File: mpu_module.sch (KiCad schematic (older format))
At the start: 1 part

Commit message: Added Mipi Dsi connection, started stlink module
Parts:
- added R7, R8: 4k7, Resistor_Smd_0603:4k7_0603, symbol Resistors_Smd0603:4k7
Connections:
- net GND: now reaches SOM1.1 (GND)
- net GND: now also SOM1.103 (GND), SOM1.107 (GND), SOM1.115 (GND), SOM1.116 (GND), SOM1.120 (GND), SOM1.125 (GND), SOM1.127 (GND), SOM1.128 (GND), SOM1.130 (GND), SOM1.132 (GND), SOM1.135 (GND), SOM1.136 (GND), SOM1.146 (GND), SOM1.147 (GND), SOM1.15 (GND), SOM1.156 (GND), SOM1.159 (GND), SOM1.165 (GND), SOM1.168 (GND), SOM1.17 (GND), SOM1.170 (GND), SOM1.172 (GND), SOM1.174 (GND), SOM1.176 (GND), SOM1.177 (GND), SOM1.178 (GND), SOM1.180 (GND), SOM1.181 (GND), SOM1.182 (GND), SOM1.184 (GND), SOM1.185 (GND), SOM1.189 (GND), SOM1.199 (GND), SOM1.2 (GND), SOM1.20 (GND), SOM1.200 (GND), SOM1.22 (GND), SOM1.23 (GND), SOM1.26 (GND), SOM1.28 (GND), SOM1.29 (GND), SOM1.35 (GND), SOM1.38 (GND), SOM1.40 (GND), SOM1.41 (GND), SOM1.50 (GND), SOM1.51 (GND), SOM1.59 (GND), SOM1.60 (GND), SOM1.70 (GND), SOM1.71 (GND), SOM1.81 (GND), SOM1.82 (GND), SOM1.84 (GND)
- net at SOM1.100 (+5VIN): now also SOM1.102 (+5VIN), SOM1.104 (+5VIN), SOM1.106 (+5VIN), SOM1.108 (+5VIN), SOM1.110 (+5VIN), SOM1.112 (+5VIN), SOM1.96 (+5VIN), SOM1.98 (+5VIN)
- net at SOM1.85 (+3.3VOUT): now also SOM1.87 (+3.3VOUT), SOM1.88 (+3.3VOUT), SOM1.89 (+3.3VOUT), SOM1.90 (+3.3VOUT), SOM1.91 (+3.3VOUT), SOM1.92 (+3.3VOUT), SOM1.93 (+3.3VOUT)
- net PA14_IRQ: now reaches SOM1.117 (PA14_DBTRGO,DBTRGI,MCO2,EVENTOUT)
- net PA1_GPIO: now reaches SOM1.157 (PA1_ETH_CLK,TIM2_CH2,TIM5_CH2,LPTIM3_OUT,TIM15_CH1N,USART2_RTS/USART2_DE,UART4_RX,QUADSPI_BK1_IO3,SAI2_MCLK_B,ETH1_GMII_RX_CLK/ETH1_MII_RX_CLK/ETH1_RGMII_RX_CLK/ETH1_RMII_REF_CLK,LCD_R2,EVENTOUT,ADC1_INP17,ADC1_INN16)
- net PE2_I2C4_SDA: now reaches SOM1.56 (PB7_TIM17_CH1N,TIM4_CH2,I2C1_SDA,I2C4_SDA,USART1_RX,SDMMC2_D1,DFSDM1_CKIN5,FMC_NL,DCMI_VSYNC,EVENTOUT)
- net PE2_I2C4_SDA: now also R7.2
- net PE2_I2C4_SCL: now reaches SOM1.121 (PE2_TRACECLK,SAI1_CK1,I2C4_SCL,SPI4_SCK,SAI1_MCLK_A,QUADSPI_BK1_IO2,ETH1_GMII_TXD3/ETH1_MII_TXD3/ETH1_RGMII_TXD3,FMC_A23,EVENTOUT)
- net PE2_I2C4_SCL: now also R8.2
- net MIPI_DSI_D0_N: now reaches SOM1.186 (DSI_D0N)
- net MIPI_DSI_D0_P: now reaches SOM1.188 (DSI_D0P)
- net MIPI_DSI_D1_N: now reaches SOM1.192 (DSI_D1N)
- net MIPI_DSI_CLK_N: now reaches SOM1.193 (DSI_CKN)
- net MIPI_DSI_D1_P: now reaches SOM1.194 (DSI_D1P)
- net MIPI_DSI_CLK_P: now reaches SOM1.195 (DSI_CKP)
- new net 3V3: R7.1, R8.1
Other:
- moved on the sheet: SOM1A, SOM1D, SOM1E, SOM1F, SOM1G, SOM1H

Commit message: Schematic finished, elements figurated on pcb, tracking started
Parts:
- added C55, C56: 100n, Capacitors_Smd_0603:100nF_0603, symbol Capacitors_Smd0603:100n
- added R51, R52, R53, R54, R55, R56: 10k, Resistor_Smd_0603:10k_0603, symbol Resistors_Smd0603:10k
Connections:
- net 3V3: now also R51.1, R53.1, R55.1
- net 5V: now also SOM1.100 (+5VIN), SOM1.102 (+5VIN), SOM1.104 (+5VIN), SOM1.106 (+5VIN), SOM1.108 (+5VIN), SOM1.110 (+5VIN), SOM1.112 (+5VIN), SOM1.96 (+5VIN), SOM1.98 (+5VIN)
- net GND: now also C55.2, C56.2, R52.2, R54.2, R56.2
- net PD13_MIPI_DSI_TE: now also SOM1.49 (PD13_LPTIM1_OUT,TIM4_CH2,I2C4_SDA,I2C1_SDA,I2S3_MCK,QUADSPI_BK1_IO3,SAI2_SCK_A,FMC_A18,DSI_TE,EVENTOUT)
- net PD15_TIM4_PWM_CH4: now also SOM1.111 (PD15_TIM4_CH4,SAI3_MCLK_A,UART8_CTS,FMC_D1/FMC_DA1,LCD_R1,EVENTOUT)
- net at SOM1.6 (VDD_3V3): now also C55.1
- net at SOM1.8 (VDD_COIN_3V): now also C56.1
- net at SOM1.10 (BOOT2): now also R55.2, R56.1
- net STM32-~RST~: now reaches SOM1.4 (STM32_nRST)
- net JTAG-TMS: now reaches SOM1.46 (JTAG_TMS)
- net JTAG-~TRST~: now reaches SOM1.48 (JTAG_nTRST)
- net JTAG-TDO: now reaches SOM1.52 (JTAG_TDO)
- net JTAG-TCK: now reaches SOM1.54 (JTAG_TCK)
- net at SOM1.7 (BOOT1): now also R53.2, R54.1
- net at SOM1.9 (BOOT0): now also R51.2, R52.1
- net USB-OTG1-D_P: now reaches SOM1.19 (USB_OTG1_DP)
- net USB-OTG1-D_M: now reaches SOM1.21 (USB_OTG1_DN)
- net USB-OTG2-D_P: now reaches SOM1.25 (USB_OTG2_DP)
- net USB-OTG2-D_M: now reaches SOM1.27 (USB_OTG2_DN)
- net ENET1-CRS-DV: now reaches SOM1.101 (PA7_TIM1_CH1N,TIM3_CH2,TIM8_CH1N,SAI4_D1,SPI1_MOSI/I2S1_SDO,SPI6_MOSI,TIM14_CH1,QUADSPI_CLK,ETH1_GMII_RX_DV/ETH1_MII_RX_DV/ETH1_RGMII_RX_CTL/ETH1_RMII_CRS_DV,SAI4_SD_A,_EVENTOUT,ADC1_INP7,ADC1_INN3,ADC2_INP7,ADC2_INN3)
- net PA13-GPIO: now reaches SOM1.113 (PA13_DBTRGO,DBTRGI,MCO1,UART4_TX,EVENTOUT,BOOTFAILN)
- net PA9-GPIO: now reaches SOM1.129 (PA9_TIM1_CH2,I2C3_SMBA,SPI2_SCK/I2S2_CK,USART1_TX,SDMMC2_CDIR,SDMMC2_D5,DCMI_D0,LCD_R5,EVENTOUT)
- net PA8-GPIO: now reaches SOM1.131 (PA8_MCO1,TIM1_CH1,TIM8_BKIN2,I2C3_SCL,SPI3_MOSI/I2S3_SDO,USART1_CK,SDMMC2_CKIN,SDMMC2_D4,OTG_FS_SOF/OTG_HS_SOF,SAI4_SD_B,UART7_RX,LCD_R6,EVENTOUT,)
- net ADC1_INP19: now reaches SOM1.140 (PA5_TIM2_CH1/TIM2_ETR,TIM8_CH1N,SAI4_CK1,SPI1_SCK/I2S1_CK,SPI6_SCK,SAI4_MCLK_A,LCD_R4,EVENTOUT,ADC1_INP19,ADC1_INN18,ADC2_INP19,ADC2_INN18,DAC_OUT2)
- net ADC1_INP15: now reaches SOM1.149 (PA3_TIM2_CH4,TIM5_CH4,LPTIM5_OUT,TIM15_CH2,USART2_RX,LCD_B2,ETH1_GMII_COL/ETH1_MII_COL,LCD_B5,EVENTOUT,ADC1_INP15,PVD_IN)
- net ADC1_INP3: now reaches SOM1.152 (PA6_TIM1_BKIN,TIM3_CH1,TIM8_BKIN,SAI4_CK2,SPI1_MISO/I2S1_SDI,SPI6_MISO,TIM13_CH1,MDIOS_MDC,SAI4_SCK_A,DCMI_PIXCLK,LCD_G2,EVENTOUT,ADC1_INP3,ADC2_INP3)
- net SPI1_NSS: now reaches SOM1.162 (PA4_HDP0,TIM5_ETR,SAI4_D2,SPI1_NSS/I2S1_WS,SPI3_NSS/I2S3_WS,USART2_CK,SPI6_NSS,SAI4_FS_A,DCMI_HSYNC,LCD_VSYNC,EVENTOUT,ADC1_INP18,ADC2_INP18,DAC_OUT1)
- net ENET1-MDIO: now reaches SOM1.61 (PA2_TIM2_CH3,TIM5_CH3,LPTIM4_OUT,TIM15_CH1,USART2_TX,SAI2_SCK_B,SDMMC2_D0DIR,_ETH1_MDIO,_MDIOS_MDIO,_LCD_R1,_EVENTOUT,_ADC1_INP14,_WKUP2)
- net PA0-GPIO: now reaches SOM1.62 (PA0_TIM2_CH1/TIM2_ETR,TIM5_CH1,TIM8_ETR,TIM15_BKIN,USART2_CTS/USART2_NSS,UART4_TX,SDMMC2_CMD,SAI2_SD_B,ETH1_GMII_CRS/ETH1_MII_CRS,EVENTOUT)
- net SPI3_NSS: now reaches SOM1.69 (PA10_TIM1_CH3,SPI3_NSS/I2S3_WS,USART1_RX,MDIOS_MDIO,SAI4_FS_B,DCMI_D1,LCD_B1,EVENTOUT,OTG_FS_ID,OTG_HS_ID)
- net I2C6-SCL: now reaches SOM1.76 (PA11_TIM1_CH4,I2C6_SCL,I2C5_SCL,SPI2_NSS/I2S2_WS,UART4_RX,USART1_CTS/USART1_NSS,FDCAN1_RX,LCD_R4,EVENTOUT,OTG_FS_DM)
- net I2C6-SDA: now reaches SOM1.80 (PA12_TIM1_ETR,I2C6_SDA,I2C5_SDA,UART4_TX,USART1_RTS/USART1_DE,SAI2_FS_B,FDCAN1_TX,LCD_R5,EVENTOUT,OTG_FS_DP)
- net ENET1-TX-EN: now reaches SOM1.114 (PB11_TIM2_CH4,LPTIM2_ETR,I2C2_SDA,DFSDM1_CKIN7,USART3_RX,ETH1_GMII_TX_EN/ETH1_MII_TX_EN/ETH1_RGMII_TX_CTL/ETH1_RMII_TX_EN,DSI_TE,LCD_G5,EVENTOUT)
- net SPI1_MOSI: now reaches SOM1.118 (PB5_ETH_CLK,TIM17_BKIN,TIM3_CH2,SAI4_D1,I2C1_SMBA,SPI1_MOSI/I2S1_SDO,I2C4_SMBA,SPI3_MOSI/I2S3_SDO,SPI6_MOSI,FDCAN2_RX,SAI4_SD_A,ETH1_PPS_OUT,UART5_RX,DCMI_D10,LCD_G7,EVENTOUT)
- net ENET1-TXD1: now reaches SOM1.124 (PB13_TIM1_CH1N,DFSDM1_CKOUT,LPTIM2_OUT,SPI2_SCK/I2S2_CK,DFSDM1_CKIN1,USART3_CTS/USART3_NSS,FDCAN2_TX,ETH1_GMII_TXD1/ETH1_MII_TXD1/ETH1_RGMII_TXD1/ETH1_RMII_TXD1,UART5_TX,EVENTOUT)
- net ENET1-RXD2: now reaches SOM1.138 (PB0_TIM1_CH2N,TIM3_CH3,TIM8_CH2N,DFSDM1_CKOUT,UART4_CTS,LCD_R3,ETH1_GMII_RXD2/ETH1_MII_RXD2/ETH1_RGMII_RXD2,MDIOS_MDIO,LCD_G1,EVENTOUT,ADC1_INP9,ADC1_INN5,ADC2_INP9,ADC2_INN5)
- net ENET1-RX-ER: now reaches SOM1.150 (PB10_TIM2_CH3,LPTIM2_IN1,I2C2_SCL,SPI2_SCK/I2S2_CK,DFSDM1_DATIN7,USART3_TX,QUADSPI_BK1_NCS,ETH1_GMII_RX_ER/ETH1_MII_RX_ER,LCD_G4,EVENTOUT)
- net ENET1-TXD3: now reaches SOM1.151 (PB8_HDP6,TIM16_CH1,TIM4_CH3,DFSDM1_CKIN7,I2C1_SCL,SDMMC1_CKIN,I2C4_SCL,SDMMC2_CKIN,UART4_RX,FDCAN1_RX,SDMMC2_D4,ETH1_GMII_TXD3/ETH1_MII_TXD3/ETH1_RGMII_TXD3,SDMMC1_D4,DCMI_D6,LCD_B6,_EVENTOUT)
- net I2C1-SDA: now reaches SOM1.166 (PB9_HDP7,TIM17_CH1,TIM4_CH4,DFSDM1_DATIN7,I2C1_SDA,SPI2_NSS/I2S2_WS,I2C4_SDA,SDMMC2_CDIR,UART4_TX,FDCAN1_TX,SDMMC2_D5,SDMMC1_CDIR,SDMMC1_D5,DCMI_D7,LCD_B7,EVENTOUT)
- net USART1-TXD: now reaches SOM1.167 (PB14_TIM1_CH2N,TIM12_CH1,TIM8_CH2N,USART1_TX,SPI2_MISO/I2S2_SDI,DFSDM1_DATIN2,USART3_RTS/USART3_DE,SDMMC2_D0,EVENTOUT)
- net SPI1_MISO: now reaches SOM1.169 (PB4_TRACED8,TIM16_BKIN,TIM3_CH1,SAI4_CK2,SPI1_MISO/I2S1_SDI,SPI3_MISO/I2S3_SDI,SPI2_NSS/I2S2_WS,SPI6_MISO,SDMMC2_D3,SAI4_SCK_A,UART7_TX,EVENTOUT)
- net USART1-RXD: now reaches SOM1.171 (PB15_RTC_REFIN,TIM1_CH3N,TIM12_CH2,TIM8_CH3N,USART1_RX,SPI2_MOSI/I2S2_SDO,DFSDM1_CKIN2,SDMMC2_D1,EVENTOUT)
- net SPI1_SCK: now reaches SOM1.175 (PB3_TRACED9,TIM2_CH2,SAI4_CK1,SPI1_SCK/I2S1_CK,SPI3_SCK/I2S3_CK,SPI6_SCK,SDMMC2_D2,SAI4_MCLK_A,UART7_RX,EVENTOUT)
- net ENET1-RXD3: now reaches SOM1.58 (PB1_TIM1_CH3N,TIM3_CH4,TIM8_CH3N,DFSDM1_DATIN1,LCD_R6,ETH1_GMII_RXD3/ETH1_MII_RXD3/ETH1_RGMII_RXD3,MDIOS_MDC,LCD_G0,EVENTOUT,ADC1_INP5,ADC2_INP5)
- net I2C1-SCL: now reaches SOM1.73 (PB6_TIM16_CH1N,TIM4_CH1,I2C1_SCL,_CEC,I2C4_SCL,USART1_TX,FDCAN2_TX,QUADSPI_BK1_NCS,DFSDM1_DATIN5,UART5_TX,DCMI_D5,EVENTOUT)
- net UART4-RXD: now reaches SOM1.77 (PB2_TRACED4,RTC_OUT2,SAI1_D1,DFSDM1_CKIN1,USART1_RX,I2S_CKIN,SAI1_SD_A,SPI3_MOSI/I2S3_SDO,UART4_RX,QUADSPI_CLK,EVENTOUT)
- net ENET1-TXD2: now reaches SOM1.119 (PC2_DFSDM1_CKIN1,SPI2_MISO/I2S2_SDI,DFSDM1_CKOUT,ETH1_GMII_TXD2/ETH1_MII_TXD2/ETH1_RGMII_TXD2,DCMI_PIXCLK,EVENTOUT,ADC1_INP12,ADC1_INN11)
- net SPI3_SCK: now reaches SOM1.137 (PC10_TRACED2,DFSDM1_CKIN5,SPI3_SCK/I2S3_CK,USART3_TX,UART4_TX,QUADSPI_BK1_IO1,SAI4_MCLK_B,SDMMC1_D2,DCMI_D8,LCD_R2,EVENTOUT)
- net PC7-GPIO: now reaches SOM1.141 (PC7_HDP4,TIM3_CH2,TIM8_CH2,DFSDM1_DATIN3,I2S3_MCK,USART6_RX,SDMMC1_D123DIR,SDMMC2_D123DIR,SDMMC2_D7,SDMMC1_D7,DCMI_D1,LCD_G6,EVENTOUT)
- net PC6-GPIO: now reaches SOM1.160 (PC6_HDP1,TIM3_CH1,TIM8_CH1,DFSDM1_CKIN3,I2S2_MCK,USART6_TX,SDMMC1_D0DIR,SDMMC2_D0DIR,SDMMC2_D6,DSI_TE,SDMMC1_D6,DCMI_D0,LCD_HSYNC,EVENTOUT)
- net ADC1_INP13: now reaches SOM1.47 (PC3_TRACECLK,DFSDM1_DATIN1,SPI2_MOSI/I2S2_SDO,ETH1_GMII_TX_CLK/ETH1_MII_TX_CLK,EVENTOUT,ADC1_INP13,ADC1_INN12)
- net ENET1-MDC: now reaches SOM1.53 (PC1_TRACED0,SAI1_D1,DFSDM1_DATIN0,DFSDM1_CKIN4,SPI2_MOSI/I2S2_SDO,SAI1_SD_A,SDMMC2_CK,ETH1_MDC,MDIOS_MDC,EVENTOUT,ADC1_INP11,ADC1_INN10,ADC2_INP11,ADC2_INN10,TAMP_IN3,WKUP6)
- net ADC2_INP10: now reaches SOM1.55 (PC0_DFSDM1_CKIN0,LPTIM2_IN2,DFSDM1_DATIN4,SAI2_FS_B,QUADSPI_BK2_NCS,LCD_R5,EVENTOUT,ADC1_INP10,ADC2_INP10)
- net ENET1-RXD0: now reaches SOM1.97 (PC4_DFSDM1_CKIN2,I2S1_MCK,SPDIFRX_IN2,ETH1_GMII_RXD0/ETH1_MII_RXD0/ETH1_RGMII_RXD0/ETH1_RMII_RXD0,EVENTOUT,ADC1_INP4,ADC2_INP4)
- net ENET1-RXD1: now reaches SOM1.99 (PC5_SAI1_D3,DFSDM1_DATIN2,SAI4_D4,_SAI1_D4,SPDIFRX_IN3,ETH1_GMII_RXD1/ETH1_MII_RXD1/ETH1_RGMII_RXD1/ETH1_RMII_RXD1,_SAI4_D3,EVENTOUT,ADC1_INP8,ADC1_INN4,ADC2_INP8,ADC2_INN4)
- net SPI3_MISO: now reaches SOM1.154 (PD10_RTC_REFIN,TIM16_BKIN,DFSDM1_CKOUT,I2C5_SMBA,SPI3_MISO/I2S3_SDI,SAI3_FS_B,USART3_CK,FMC_D15/FMC_DA15,LCD_B3,EVENTOUT)
- net SPI3_MOSI: now reaches SOM1.164 (PD6_TIM16_CH1N,SAI1_D1,DFSDM1_CKIN4,DFSDM1_DATIN1,SPI3_MOSI/I2S3_SDO,SAI1_SD_A,USART2_RX,FMC_NWAIT,DCMI_D10,LCD_B2,EVENTOUT)
- net PD8-GPIO: now reaches SOM1.65 (PD8_DFSDM1_CKIN3,SAI3_SCK_B,USART3_TX,SPDIFRX_IN1,FMC_D13/FMC_DA13,LCD_B7,EVENTOUT)
- net UART8-CTS: now reaches SOM1.66 (PD14_TIM4_CH3,_SAI3_MCLK_B,UART8_CTS,FMC_AD0/FMC_D0,_EVENTOUT)
- net PD9-GPIO: now reaches SOM1.67 (PD9_DFSDM1_DATIN3,SAI3_SD_B,USART3_RX,FMC_D14/FMC_DA14,DCMI_HSYNC,LCD_B0,EVENTOUT)
- net PD11-GPIO: now reaches SOM1.72 (PD11_LPTIM2_IN2,I2C4_SMBA,I2C1_SMBA,USART3_CTS/USART3_NSS,QUADSPI_BK1_IO0,SAI2_SD_A,FMC_CLE/FMC_A16,EVENTOUT)
- net PD12-GPIO: now reaches SOM1.78 (PD12_LPTIM1_IN1,TIM4_CH1,LPTIM2_IN1,I2C4_SCL,I2C1_SCL,USART3_RTS/USART3_DE,QUADSPI_BK1_IO1,SAI2_FS_A,FMC_ALE/FMC_A17,EVENTOUT)
- net PE15-GPIO: now reaches SOM1.134 (PE15_HDP3,TIM1_BKIN,TIM15_BKIN,USART2_CTS/USART2_NSS,UART8_CTS,FMC_NCE2,FMC_D12/FMC_DA12,LCD_R7,EVENTOUT)
- net PE11-GPIO: now reaches SOM1.148 (PE11_TIM1_CH2,DFSDM1_CKIN4,SPI4_NSS,USART6_CK,SAI2_SD_B,FMC_D8/FMC_DA8,DCMI_D4,LCD_G3,EVENTOUT)
- net PE12-GPIO: now reaches SOM1.158 (PE12_TIM1_CH3N,DFSDM1_DATIN5,SPI4_SCK,SDMMC1_D0DIR,SAI2_SCK_B,FMC_D9/FMC_DA9,LCD_B4,EVENTOUT)
- net PE14-GPIO: now reaches SOM1.161 (PE14_TIM1_CH4,SPI4_MOSI,UART8_RTS/UART8_DE,SAI2_MCLK_B,SDMMC1_D123DIR,FMC_D11/FMC_DA11,LCD_G0,LCD_CLK,EVENTOUT)
- net PE13-GPIO: now reaches SOM1.163 (PE13_HDP2,TIM1_CH3,DFSDM1_CKIN5,SPI4_MISO,SAI2_FS_B,FMC_D10/FMC_DA10,DCMI_D6,LCD_DE,EVENTOUT)
- net PE3-GPIO: now reaches SOM1.179 (PE3_TRACED0,TIM15_BKIN,SAI1_SD_B,SDMMC2_CK,FMC_A19,EVENTOUT)
- net UART8-TXD: now reaches SOM1.57 (PE1_LPTIM1_IN2,I2S2_MCK,SAI3_SD_B,UART8_TX,FMC_NBL1,DCMI_D3,EVENTOUT)
- net UART8-RXD: now reaches SOM1.63 (PE0_LPTIM1_ETR,TIM4_ETR,LPTIM2_ETR,SPI3_SCK/I2S3_CK,SAI4_MCLK_B,UART8_RX,SAI2_MCLK_A,FMC_NBL0,DCMI_D2,EVENTOUT)
- net PG12-GPIO: now reaches SOM1.109 (PG12_LPTIM1_IN1,SPI6_MISO,SAI4_CK2,USART6_RTS/USART6_DE,SPDIFRX_IN1,LCD_B4,SAI4_SCK_A,ETH1_PHY_INTN,FMC_NE4,LCD_B1,EVENTOUT)
- net PG13-GPIO: now reaches SOM1.122 (PG13_TRACED0,LPTIM1_OUT,SAI1_CK2,SAI4_CK1,SPI6_SCK,SAI1_SCK_A,USART6_CTS/USART6_NSS,SAI4_MCLK_A,ETH1_GMII_TXD0/ETH1_MII_TXD0/ETH1_RGMII_TXD0/ETH1_RMII_TXD0,FMC_A24,LCD_R0,EVENTOUT)
- net ADC1_INP2: now reaches SOM1.139 (PF11_SPI5_MOSI,SAI2_SD_B,DCMI_D12,LCD_G5,EVENTOUT,ADC1_INP2)
- net PG6-GPIO: now reaches SOM1.173 (PG6_TRACED14,TIM17_BKIN,SDMMC2_CMD,DCMI_D12,LCD_R7,EVENTOUT)
- net PG10-GPIO: now reaches SOM1.45 (PG10_TRACED10,UART8_CTS,LCD_G3,SAI2_SD_B,QUADSPI_BK2_IO2,FMC_NE3,DCMI_D2,LCD_B2,EVENTOUT)
- net PF10-GPIO: now reaches SOM1.64 (PF10_PF10_TIM16_BKIN,SAI1_D3,SAI4_D4,SAI1_D4,QUADSPI_CLK,SAI4_D3,DCMI_D11,_LCD_DE,EVENTOUT)
- net UART8-RTS: now reaches SOM1.74 (PG7_TRACED5,_SAI1_MCLK_A,_USART6_CK,_UART8_RTS/UART8_DE,_QUADSPI_CLK,_QUADSPI_BK2_IO3,_DCMI_D13,_LCD_CLK,_EVENTOUT)
- net UART4-TXD: now reaches SOM1.75 (PG11_TRACED11,USART1_TX,UART4_TX,SPDIFRX_IN0,ETH1_GMII_TX_EN/ETH1_MII_TX_EN/ETH1_RGMII_TX_CTL/ETH1_RMII_TX_EN,DCMI_D3,LCD_B3,_EVENTOUT)
- net ENET1-TXD0: now reaches SOM1.79 (PG14_TRACED1,LPTIM1_ETR,SPI6_MOSI,_SAI4_D1,USART6_TX,QUADSPI_BK2_IO3,SAI4_SD_A,ETH1_GMII_TXD1/ETH1_MII_TXD1/ETH1_RGMII_TXD1/ETH1_RMII_TXD1,FMC_A25,LCD_B0,EVENTOUT)
- net PA1_GPIO renamed ENET1-REFCLK
- no-connect marks 0 -> 2
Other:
- moved on the sheet: R8, SOM1B, SOM1C, SOM1G, SOM1H, SOM1I, SOM1J

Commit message: Tracking in progress
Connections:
- net USB-OTG1-D_M renamed USB-OTG1-D_N
- net USB-OTG2-D_M renamed USB-OTG2-D_N
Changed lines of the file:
@@
 	1750 9750 1450 9750
 Text HLabel 1450 9750 0    50   BiDi ~ 0
-USB-OTG1-D_M
+USB-OTG1-D_N
 Wire Wire Line
 	1750 9650 1450 9650
@@
 	1750 9250 1450 9250
 Text HLabel 1450 9250 0    50   BiDi ~ 0
-USB-OTG2-D_M
+USB-OTG2-D_N
 Wire Wire Line
 	1750 9150 1450 9150

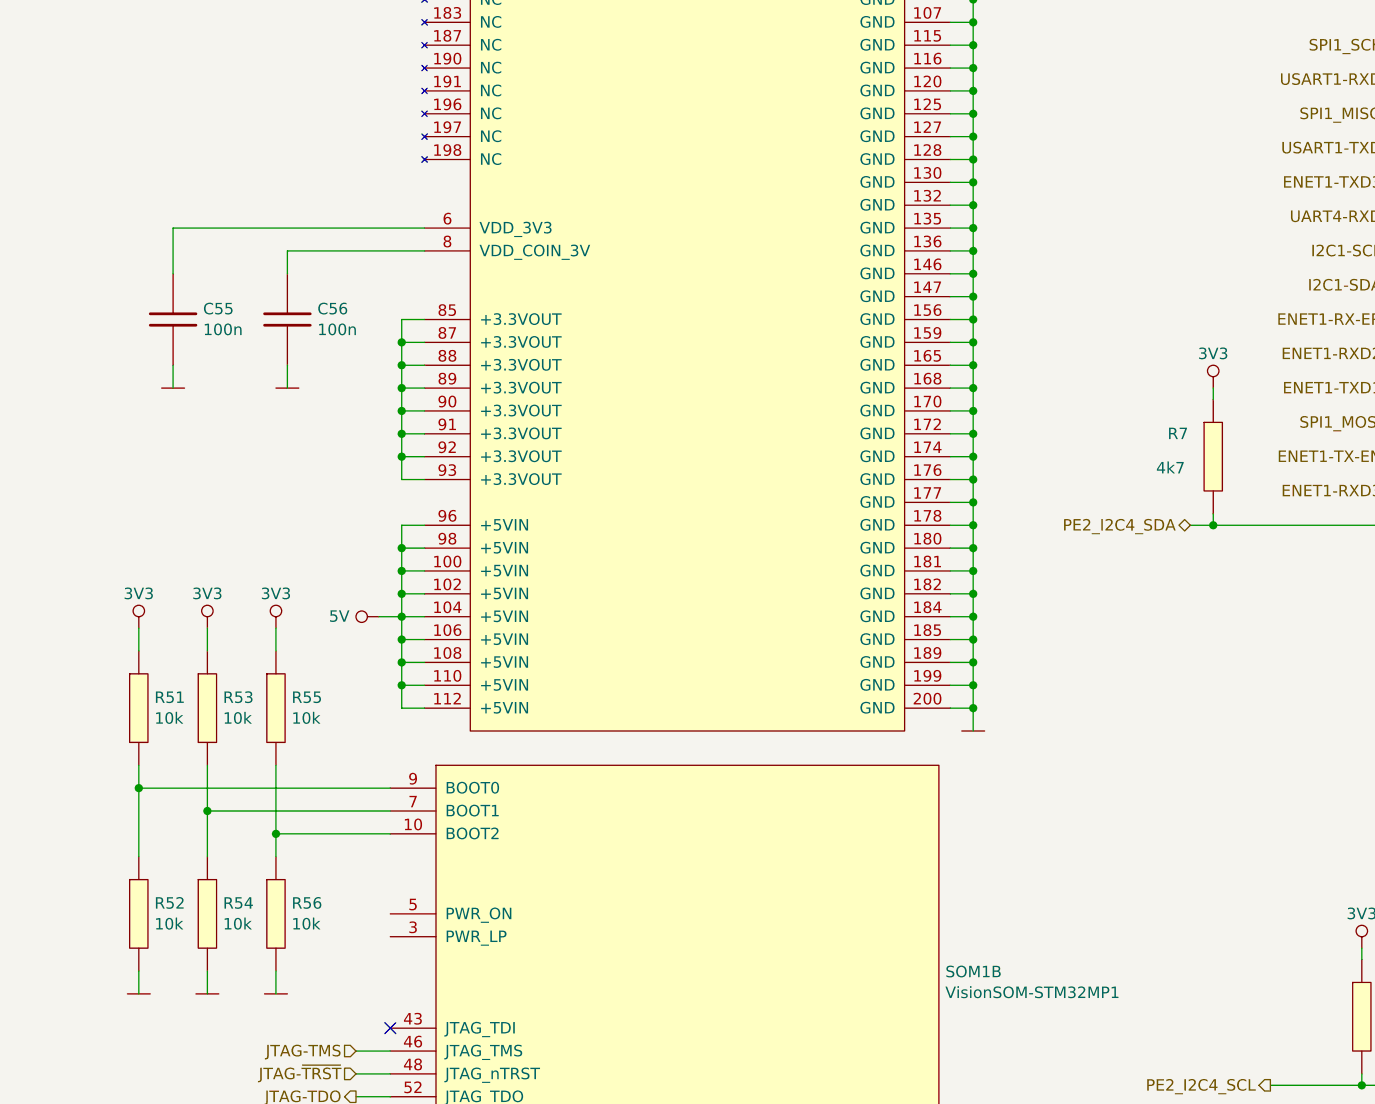
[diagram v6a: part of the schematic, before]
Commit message: Tracking finished, started tunning
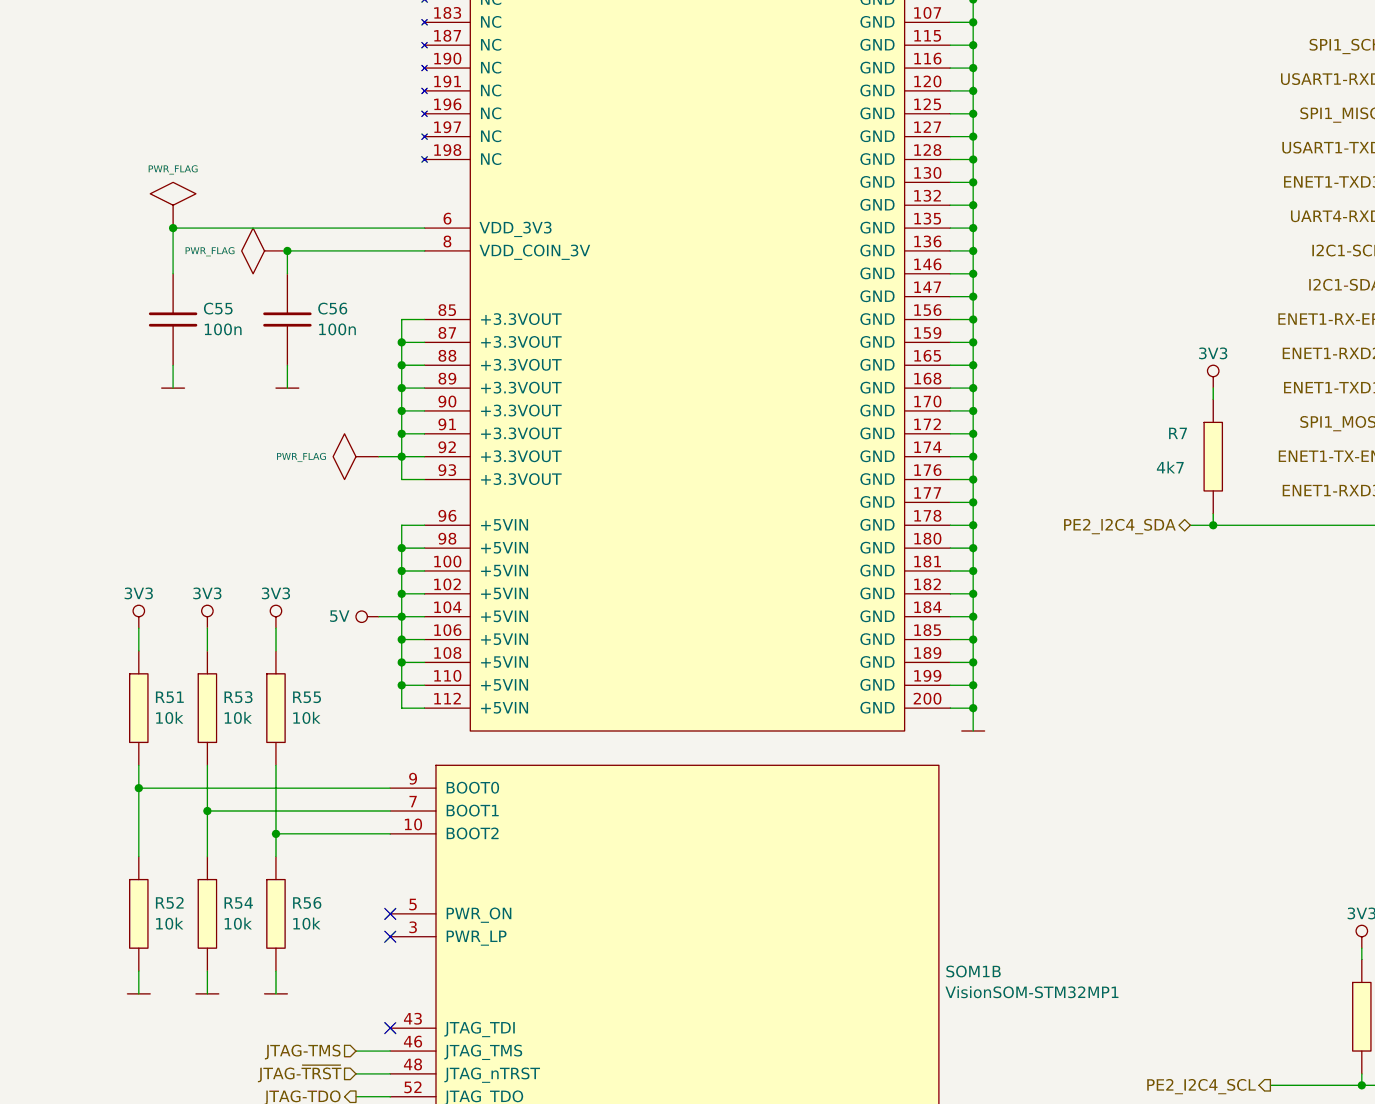
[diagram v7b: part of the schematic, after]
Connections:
- no-connect marks 2 -> 4
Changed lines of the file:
@@
 	1300 850  1200 850
-$Comp
-L power:3V3_NO_GLOBAL #PWR25
-U 1 1 5FEE9D80
-P 1300 950
-F 0 "#PWR25" H 1300 1050 40  0001 C CNN
-F 1 "3V3" V 1306 1078 50  0000 L CNN
-F 2 "" H 1300 950 60  0000 C CNN
-F 3 "" H 1300 950 60  0000 C CNN
-	1    1300 950
-	0    1    1    0
-$EndComp
-Wire Wire Line
-	1300 950  1200 950
 $Comp
 L power:3V3_NO_GLOBAL #PWR29
@@
 	1    0    0    -1
 $EndComp
-Wire Wire Line
-	5700 4850 5700 4900
 Wire Wire Line
 	6350 7300 6350 7350
@@
 Wire Wire Line
 	1150 4150 1150 4350
+$Comp
+L power:PWR_FLAG #FLG0107
+U 1 1 600E1660
+P 2050 5150
+F 0 "#FLG0107" H 2050 5420 30  0001 C CNN
+F 1 "PWR_FLAG" V 2050 5378 30  0000 L CNN
+F 2 "" H 2050 5150 60  0000 C CNN
+F 3 "" H 2050 5150 60  0000 C CNN
+	1    2050 5150
+	0    -1   -1   0
+$EndComp
+Wire Wire Line
+	2150 5150 2050 5150
+$Comp
+L power:PWR_FLAG #FLG0108
+U 1 1 600FB2D6
+P 1150 4150
+F 0 "#FLG0108" H 1150 4420 30  0001 C CNN
+F 1 "PWR_FLAG" H 1150 4408 30  0000 C CNN
+F 2 "" H 1150 4150 60  0000 C CNN
+F 3 "" H 1150 4150 60  0000 C CNN
+	1    1150 4150
+	1    0    0    -1
+$EndComp
+Connection ~ 1150 4150
+$Comp
+L power:PWR_FLAG #FLG0109
+U 1 1 600FC92B
+P 1650 4250
+F 0 "#FLG0109" H 1650 4520 30  0001 C CNN
+F 1 "PWR_FLAG" V 1650 4478 30  0000 L CNN
+F 2 "" H 1650 4250 60  0000 C CNN
+F 3 "" H 1650 4250 60  0000 C CNN
+	1    1650 4250
+	0    -1   -1   0
+$EndComp
+Connection ~ 1650 4250
+NoConn ~ 2100 7150
+NoConn ~ 2100 7250
+Wire Wire Line
+	5700 4900 5700 4850
+Wire Wire Line
+	1300 950  1200 950
+$Comp
+L power:3V3_NO_GLOBAL #PWR25
+U 1 1 5FEE9D80
+P 1300 950
+F 0 "#PWR25" H 1300 1050 40  0001 C CNN
+F 1 "3V3" V 1306 1078 50  0000 L CNN
+F 2 "" H 1300 950 60  0000 C CNN
+F 3 "" H 1300 950 60  0000 C CNN
+	1    1300 950
+	0    1    1    0
+$EndComp
 $EndSCHEMATC
